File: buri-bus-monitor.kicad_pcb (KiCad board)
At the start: 2 copper layers, 99.1 x 158.8 mm, 20 parts, among them P1 Buri-Bus, U1 74HC04, U2 74LS299, U3 74HC00, U4 74HC74, U5 74LS299, U6 74LS299, U7 74LS299, U8 Arduino Nano

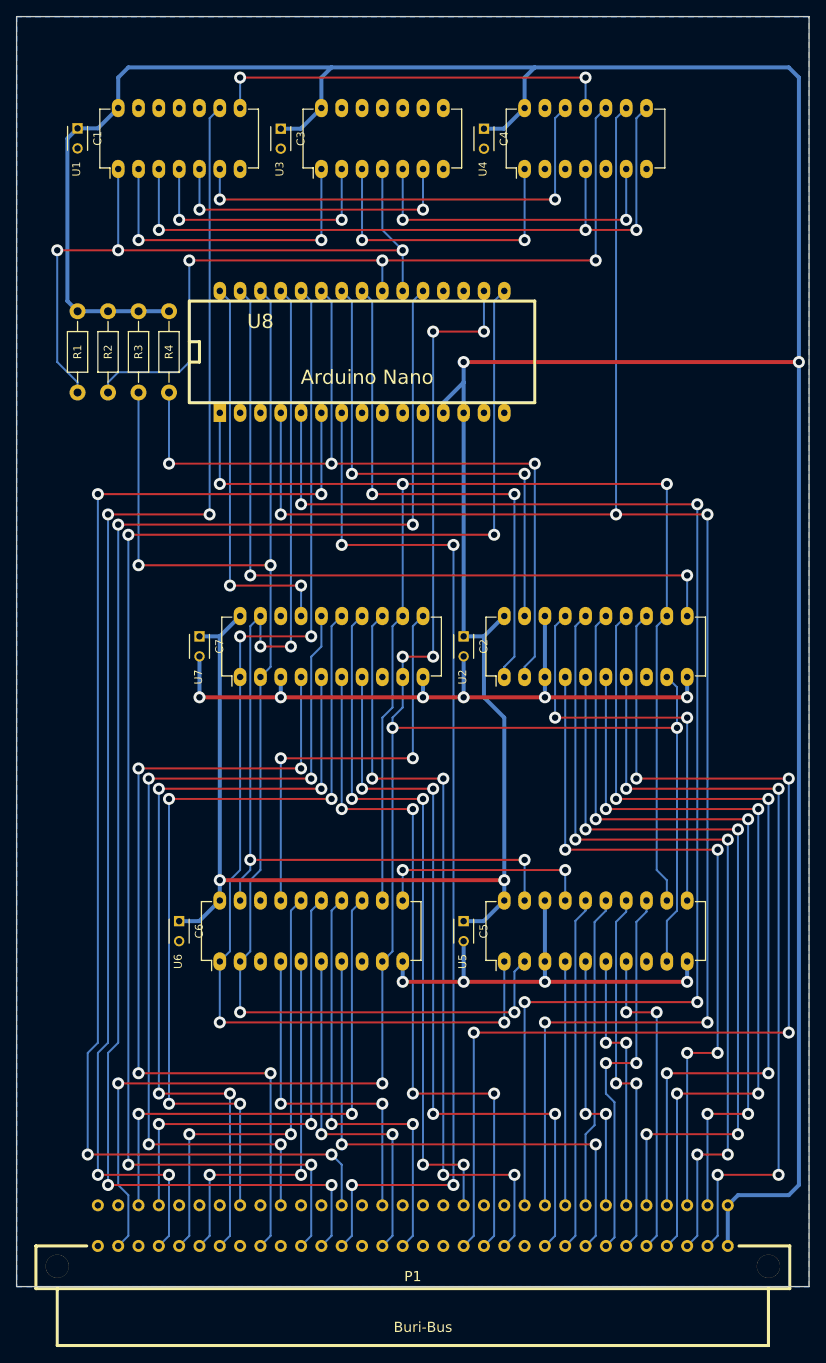
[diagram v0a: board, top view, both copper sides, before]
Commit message: correct single step logic
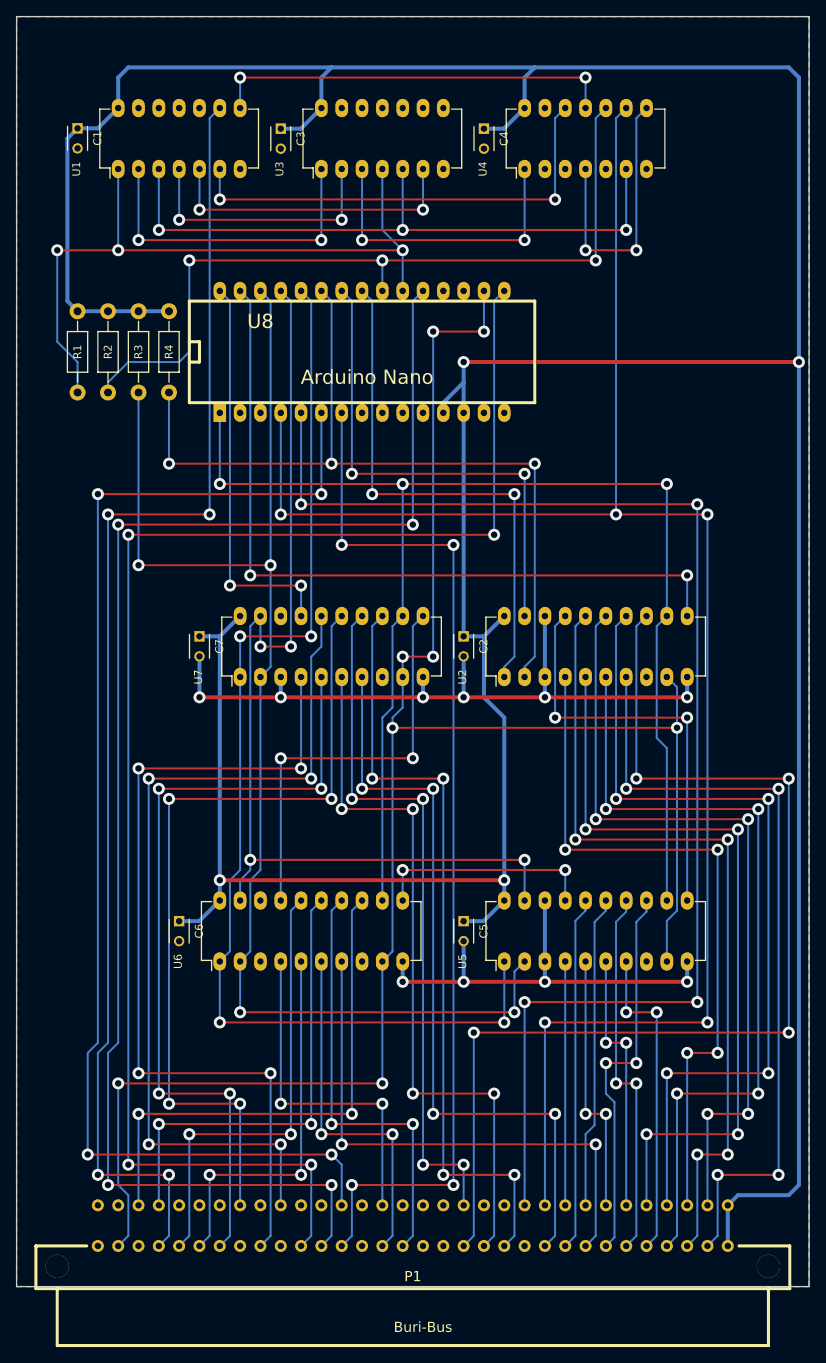
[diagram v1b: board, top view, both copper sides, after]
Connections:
- net /~IOSEL renamed Net-(P1-Pad27a)
- U3 pad 5: Net-(U3-Pad5) -> Net-(U1-Pad3)
- U4 pad 13: GND -> +5V
- U4 pad 4: Net-(U1-Pad3) -> Net-(U4-Pad4)
- U4 pad 6: Net-(U3-Pad5) -> Net-(U1-Pad3)
- U4 pad 8: Net-(U1-Pad3) -> Net-(U4-Pad4)
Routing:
- net Net-(U3-Pad5): track 40.6 -> 0.00 mm, vias 2 -> 0
- net Net-(U4-Pad4): track 0.00 -> 34.8 mm, vias 0 -> 2
- net Net-(U1-Pad3): track 90.7 -> 81.3 mm
- net /HALT: track 99.4 -> 98.6 mm
